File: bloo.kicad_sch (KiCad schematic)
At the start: 84 parts, among them M1 M1_Conn_Alt, M2 M2_Conn_Alt, Q0 TEFT4300, Q1 TEFT4300, Q10 Q_NMOS_GSD, Q11 Q_NMOS_GSD, Q12 Q_NMOS_GSD, Q2 TEFT4300, Q3 TEFT4300, Q9 Q_NMOS_GSD, SW1 SW, SW2 SW, SW3 SW, U1 YAAJ_BluePill_SWD_Breakout, U2 L293D, U3 LM1085-5.0, U4 APE8865Y5-33-HF-3

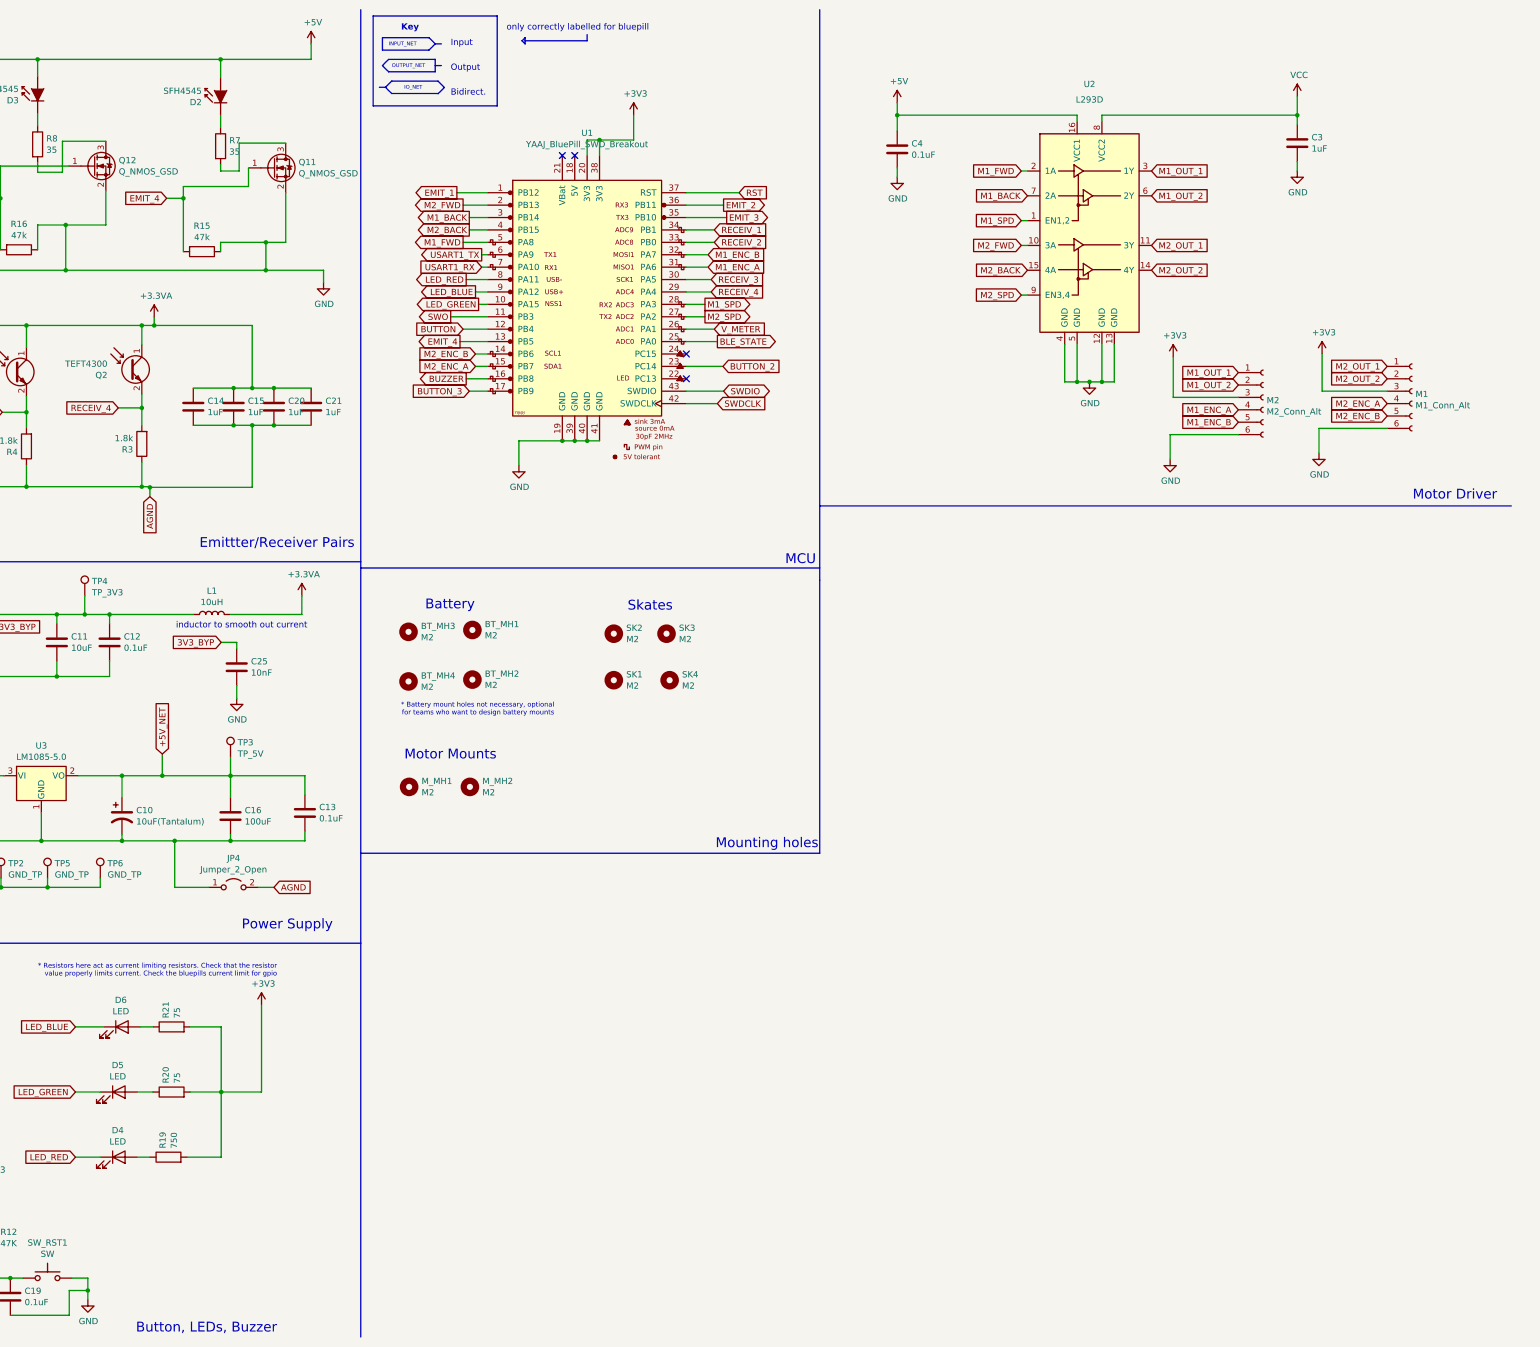
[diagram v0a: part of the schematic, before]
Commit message: added and wired bluetooth module
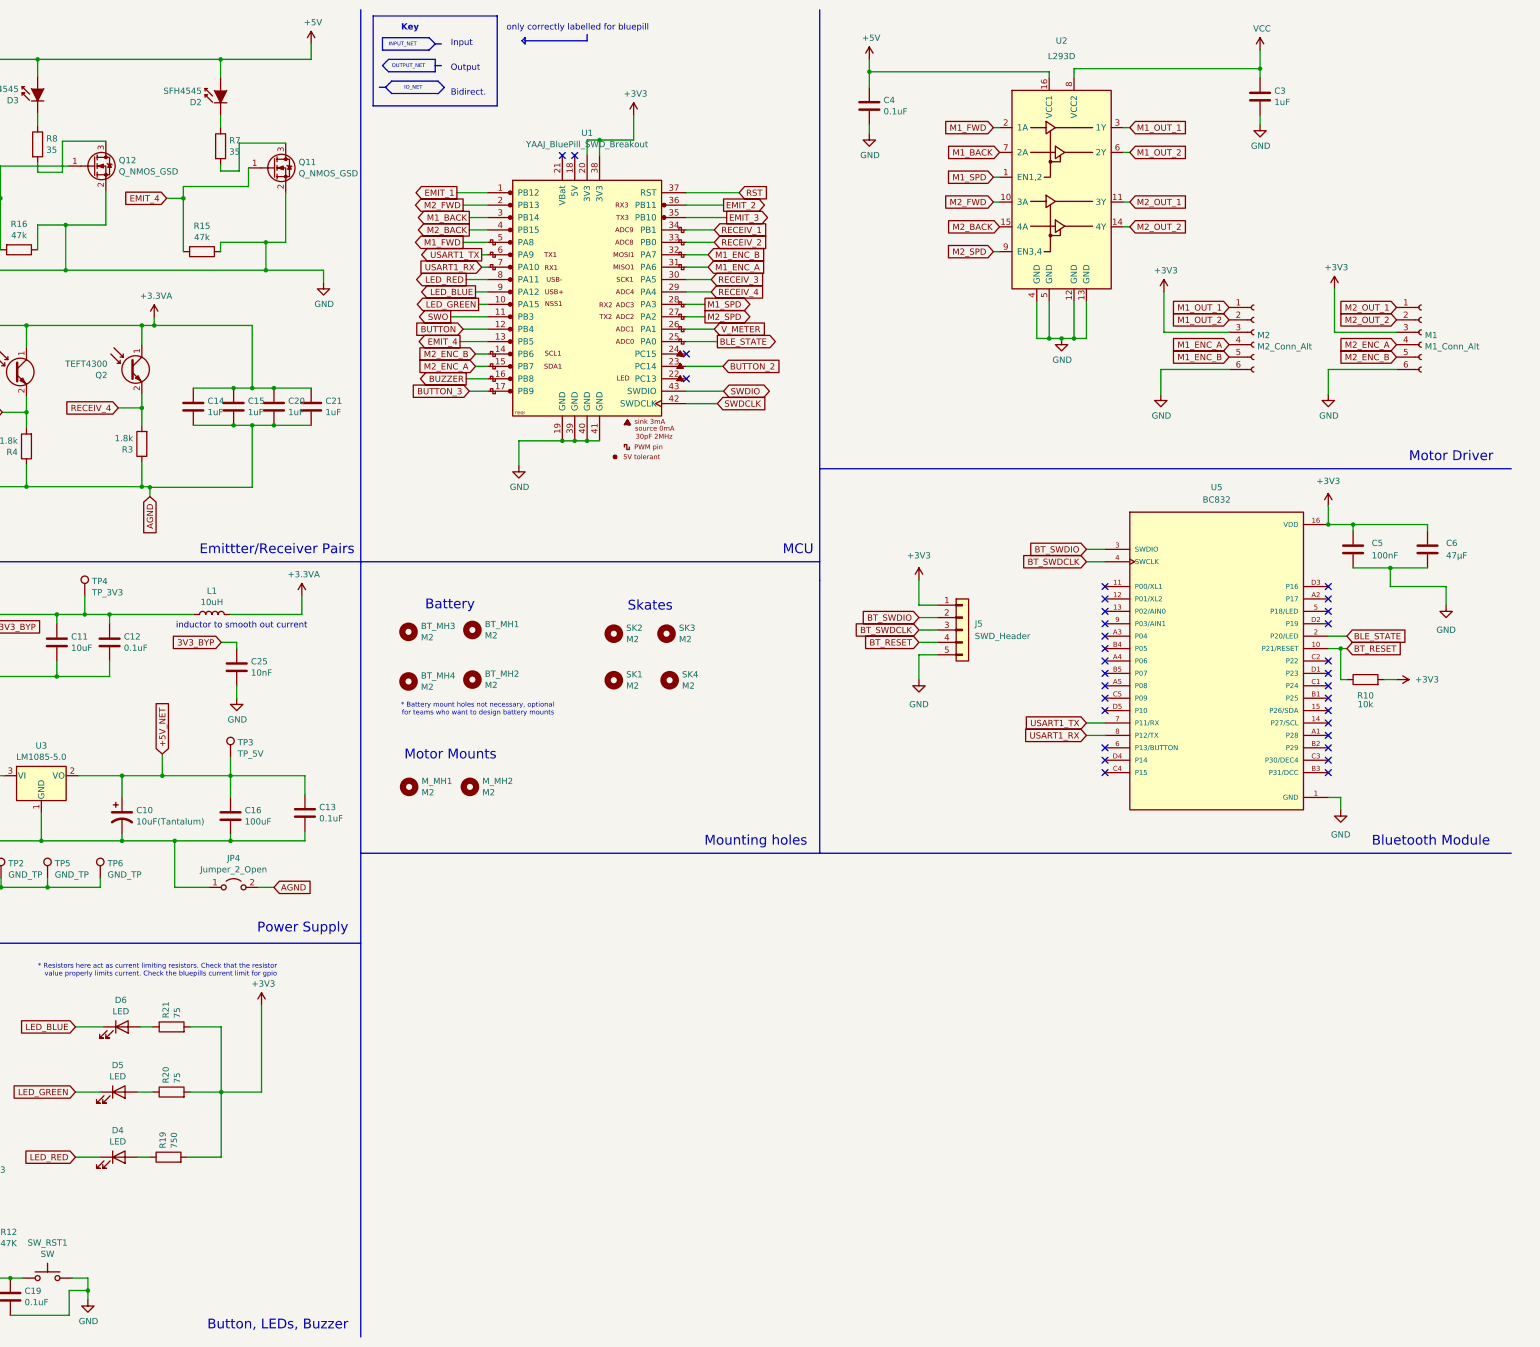
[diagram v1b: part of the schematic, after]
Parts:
- added C5: 100nF, Capacitor_SMD:C_0603_1608Metric, symbol Device:C
- added C6: 47µF, Capacitor_SMD:C_1206_3216Metric, symbol Device:C
- added J5: SWD_Header, Connector_PinHeader_2.54mm:PinHeader_1x05_P2.54mm_Vertical, symbol Connector_Generic:Conn_01x05
- added R10: 10k, Resistor_SMD:R_1206_3216Metric_Pad1.30x1.75mm_HandSolder, symbol Device:R
- added U5: BC832, custom_foot:XCVR_BC832, symbol BC832:BC832
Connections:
- net +3V3: now also C5.1, C6.1, J5.1 (Pin_1), R10.2, U5.16 (VDD)
- net BLE_STATE: now also U5.2 (P20/LED)
- net GND: now also C5.2, C6.2, J5.5 (Pin_5), U5.1 (GND)
- net USART1_RX: now also U5.8 (P12/TX)
- net USART1_TX: now also U5.7 (P11/RX)
- new net BT_RESET: J5.4 (Pin_4), R10.1, U5.10 (P21/RESET)
- new net BT_SWDCLK: J5.3 (Pin_3), U5.4 (SWCLK)
- new net BT_SWDIO: J5.2 (Pin_2), U5.3 (SWDIO)
- no-connect marks 4 -> 32
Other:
- note added: "Bluetooth Module"
- moved on the sheet: C3, C4, M1, M2, U2

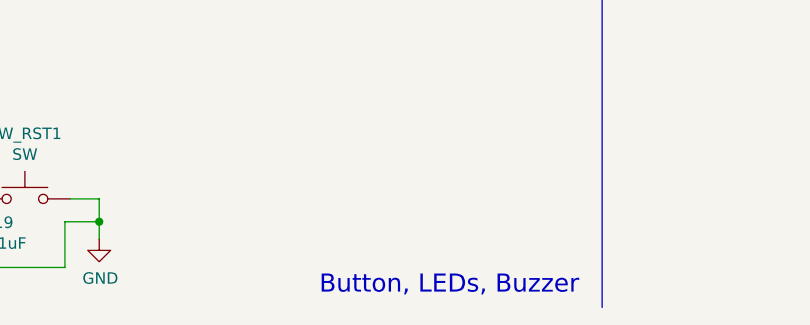
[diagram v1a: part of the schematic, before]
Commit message: edgecut edits + adding on layout
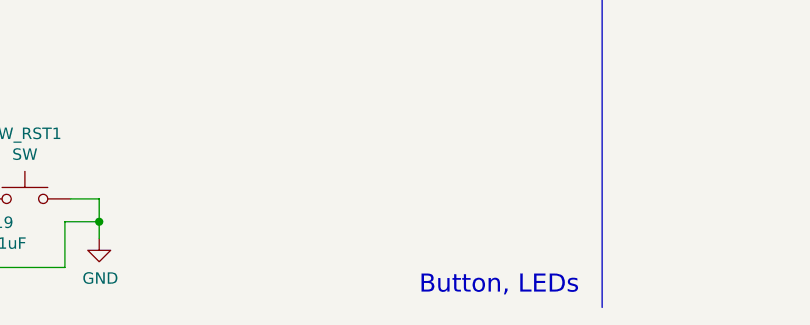
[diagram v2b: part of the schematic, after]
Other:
- note added: "Button, LEDs"
- note removed: "Button, LEDs, Buzzer"
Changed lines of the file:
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@@
 		)
 	)
-	(text "Button, LEDs, Buzzer"
+	(text "Button, LEDs\n"
 		(exclude_from_sim no)
 		(at 170.18 283.21 0)

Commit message: remove 5V net, direct LDO 5V connection
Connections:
- net +5V_NET is gone; now on net +5V: C10.1, C13.1, C16.1, TP3.1, U3.2 (VO)
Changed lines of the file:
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@@
 		)
 	)
-	(global_label "+5V_NET"
-		(shape input)
-		(at 132.08 165.1 90)
-		(fields_autoplaced yes)
-		(effects
-			(font
-				(size 1.27 1.27)
-			)
-			(justify left)
-		)
-		(property "Intersheetrefs" "${INTERSHEET_REFS}"
-			(at 132.08 154.4838 90)
-			(effects
-				(font
-					(size 1.27 1.27)
-				)
-				(justify left)
-				(hide yes)
-			)
-		)
-	)
 	(global_label "3V3_BYP"
 		(shape input)
@@
 					(unit 1)
 				)
+			)
+		)
+	)
+	(symbol
+		(lib_id "power:+5V")
+		(at 132.08 165.1 0)
+		(unit 1)
+		(exclude_from_sim no)
+		(in_bom yes)
+		(on_board yes)
+		(dnp no)
+		(property "Reference" "#PWR018"
+			(at 132.08 168.91 0)
+			(effects
+				(font
+					(size 1.27 1.27)
+				)
+				(hide yes)
+			)
+		)
+		(property "Value" "+5V"
+			(at 132.461 160.7058 0)
+			(effects
+				(font
+					(size 1.27 1.27)
+				)
+			)
+		)
+		(property "Footprint" ""
+			(at 132.08 165.1 0)
+			(effects
+				(font
+					(size 1.27 1.27)
+				)
+				(hide yes)
+			)
+		)
+		(property "Datasheet" ""
+			(at 132.08 165.1 0)
+			(effects
+				(font
+					(size 1.27 1.27)
+				)
+				(hide yes)
+			)
+		)
+		(property "Description" ""
+			(at 132.08 165.1 0)
+			(effects
+				(font
+					(size 1.27 1.27)
+				)
+			)
+		)
+		(pin "1"
+		)
+		(instances
+			(project "bloo"
+				(path "/9031bb33-c6aa-4758-bf5c-3274ed3ebab7"
+					(reference "#PWR018")
+					(unit 1)
+				)

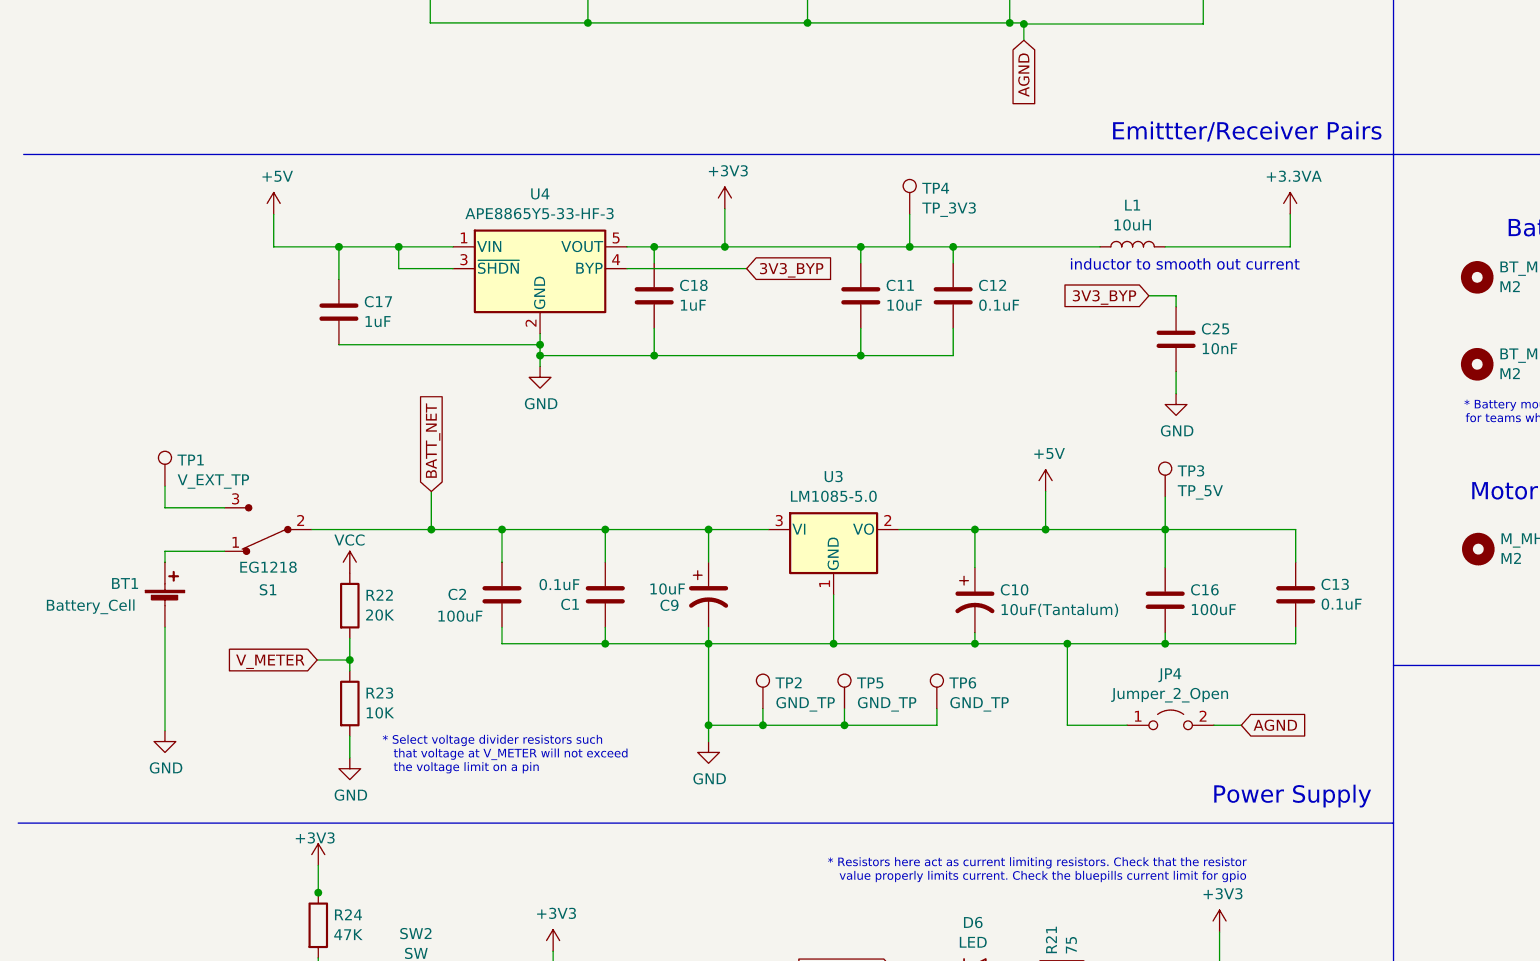
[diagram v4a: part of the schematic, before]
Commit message: connected vcc to batt_net and add power flag to power rails for erc
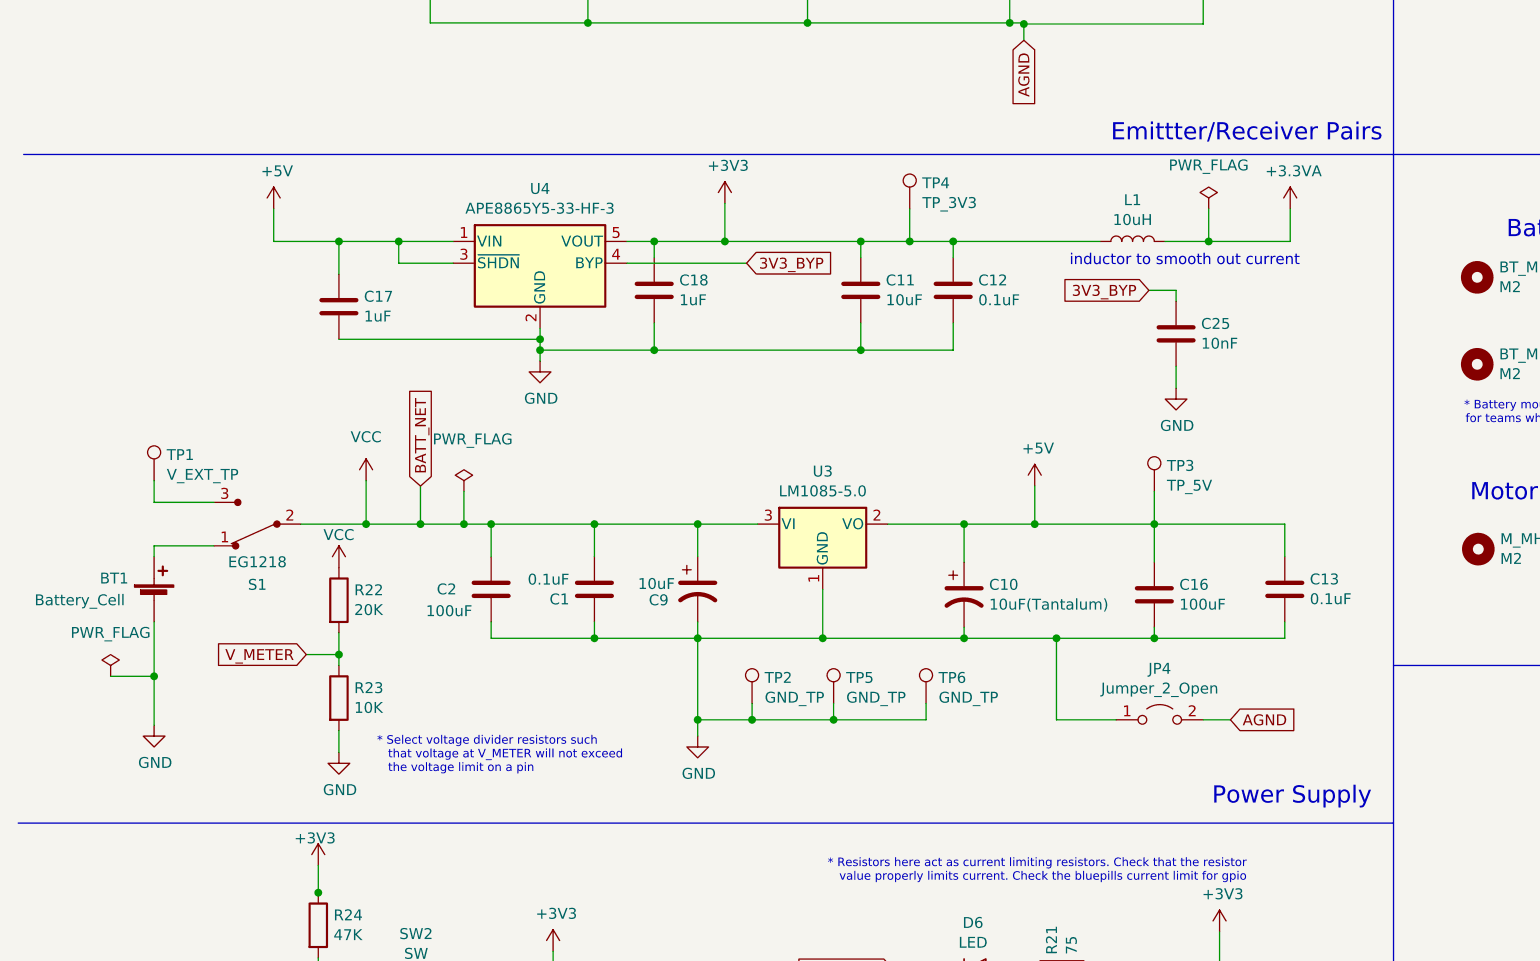
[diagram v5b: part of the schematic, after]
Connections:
- net BATT_NET is gone; now on net VCC: C1.2, C2.1, C9.1, S1.2, U3.3 (VI)
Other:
- moved on the sheet: BT1, C1, C10, C11, C12, C13, C16, C17, C18, C2, C25, C9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

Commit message: started routing
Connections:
- net SWO: no longer names the net of U1.11 (PB3)
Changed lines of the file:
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@@
 	)
 	(junction
-		(at 59.055 168.91)
-		(diameter 0)
-		(color 0 0 0 0)
-	)
-	(junction
 		(at 110.49 148.59)
 		(diameter 0)
@@
 	(wire
 		(pts
-			(xy 52.705 168.91) (xy 59.055 168.91)
-		)
-		(stroke
-			(width 0)
-			(type default)
-		)
-	)
-	(wire
-		(pts
-			(xy 198.755 75.565) (xy 191.135 75.565)
+			(xy 52.705 168.91) (xy 64.135 168.91)
 		)
 		(stroke
@@
 	(wire
 		(pts
-			(xy 59.055 168.91) (xy 64.135 168.91)
-		)
-		(stroke
-			(width 0)
-			(type default)
-		)
-	)
-	(wire
-		(pts
 			(xy 60.198 95.377) (xy 60.198 98.933)
 		)
@@
 	(wire
 		(pts
-			(xy 59.055 164.465) (xy 59.055 168.91)
-		)
-		(stroke
-			(width 0)
-			(type default)
-		)
-	)
-	(wire
-		(pts
 			(xy 97.155 267.97) (xy 97.155 272.415)
 		)
@@
 		)
 	)
-	(global_label "SWO"
-		(shape output)
-		(at 191.135 75.565 180)
-		(fields_autoplaced yes)
-		(effects
-			(font
-				(size 1.27 1.27)
-			)
-			(justify right)
-		)
-		(property "Intersheetrefs" "${INTERSHEET_REFS}"
-			(at 184.8126 75.565 0)
-			(effects
-				(font
-					(size 1.27 1.27)
-				)
-				(justify right)
-				(hide yes)
-			)
-		)
-	)
 	(global_label "M2_SPD"
 		(shape output)
@@
 				(hide yes)
 			)
-		)
-	)
-	(global_label "BATT_NET"
-		(shape input)
-		(at 59.055 164.465 90)
-		(fields_autoplaced yes)
-		(effects
-			(font
-				(size 1.27 1.27)
-			)
-			(justify left)
-		)
-		(property "Intersheetrefs" "${INTERSHEET_REFS}"
-			(at 59.055 153.4255 90)
-			(effects
-				(font
-					(size 1.27 1.27)
-				)
-				(justify left)
-				(hide yes)
-			)

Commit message: green board --> connector footprint + logo
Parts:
- M1, M2: footprint MM_Library:Motor Headers -> Connector_JST:JST_XH_B6B-XH-A_1x06_P2.50mm_Vertical
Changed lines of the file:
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@@
 			)
 		)
-		(property "Footprint" "MM_Library:Motor Headers"
+		(property "Footprint" "Connector_JST:JST_XH_B6B-XH-A_1x06_P2.50mm_Vertical"
 			(at 389.89 78.74 0)
 			(effects
@@
 			)
 		)
-		(property "Footprint" "MM_Library:Motor Headers"
+		(property "Footprint" "Connector_JST:JST_XH_B6B-XH-A_1x06_P2.50mm_Vertical"
 			(at 355.6 78.74 0)
 			(effects

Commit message: added LCSC part in BOM
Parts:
- U5: LCSC Part # (none) -> C6470192
